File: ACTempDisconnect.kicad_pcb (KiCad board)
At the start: 4 copper layers, 120 x 99.5 mm, 49 parts, among them J1001 Conn_01x03_Female, J1002 NTC_Connection, J1003 Conn_01x02_Female, J1004 Conn_01x03_Female, J1005 Conn_01x02_Female, J2001 TAG_CONNECT, K1001 ADW1103HLW, K1002 ADW1103HLW, K1003 ADW1103HLW, K1004 ADW1103HLW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

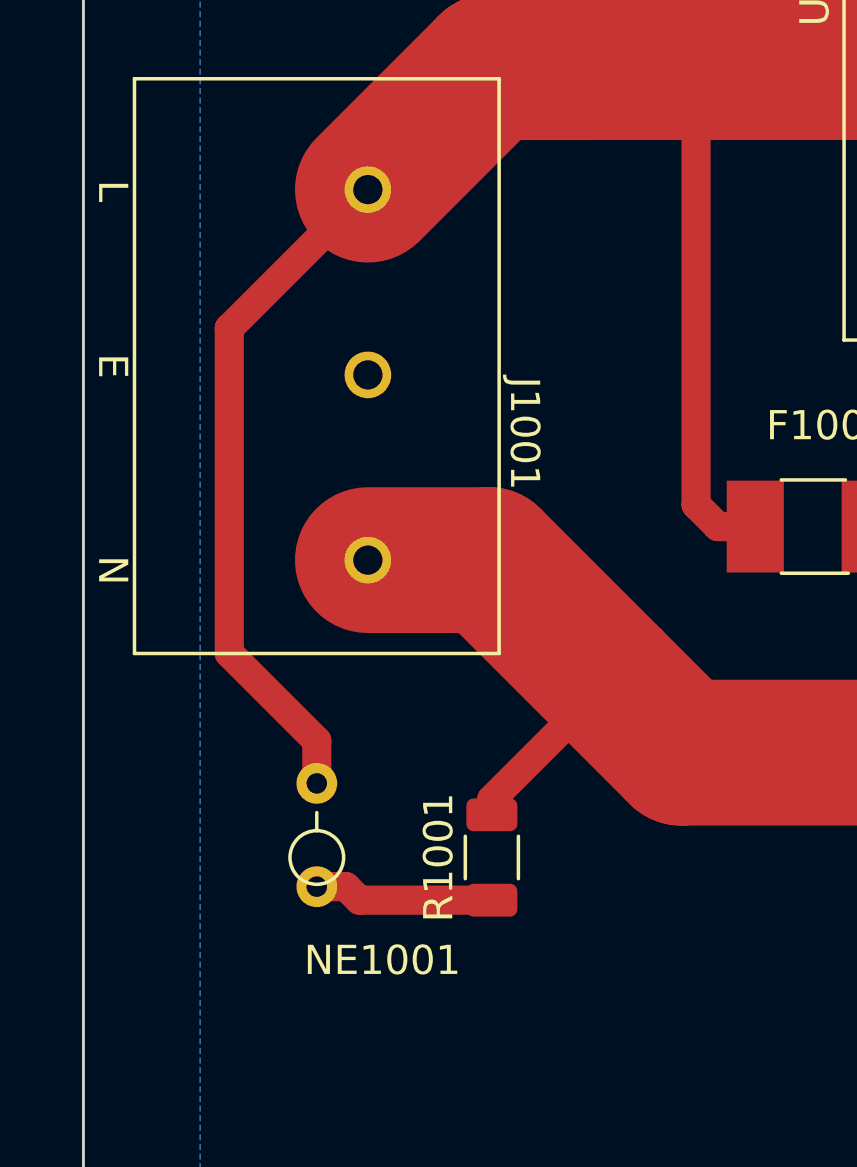
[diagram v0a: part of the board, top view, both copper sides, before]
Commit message: Removed Neon from V2
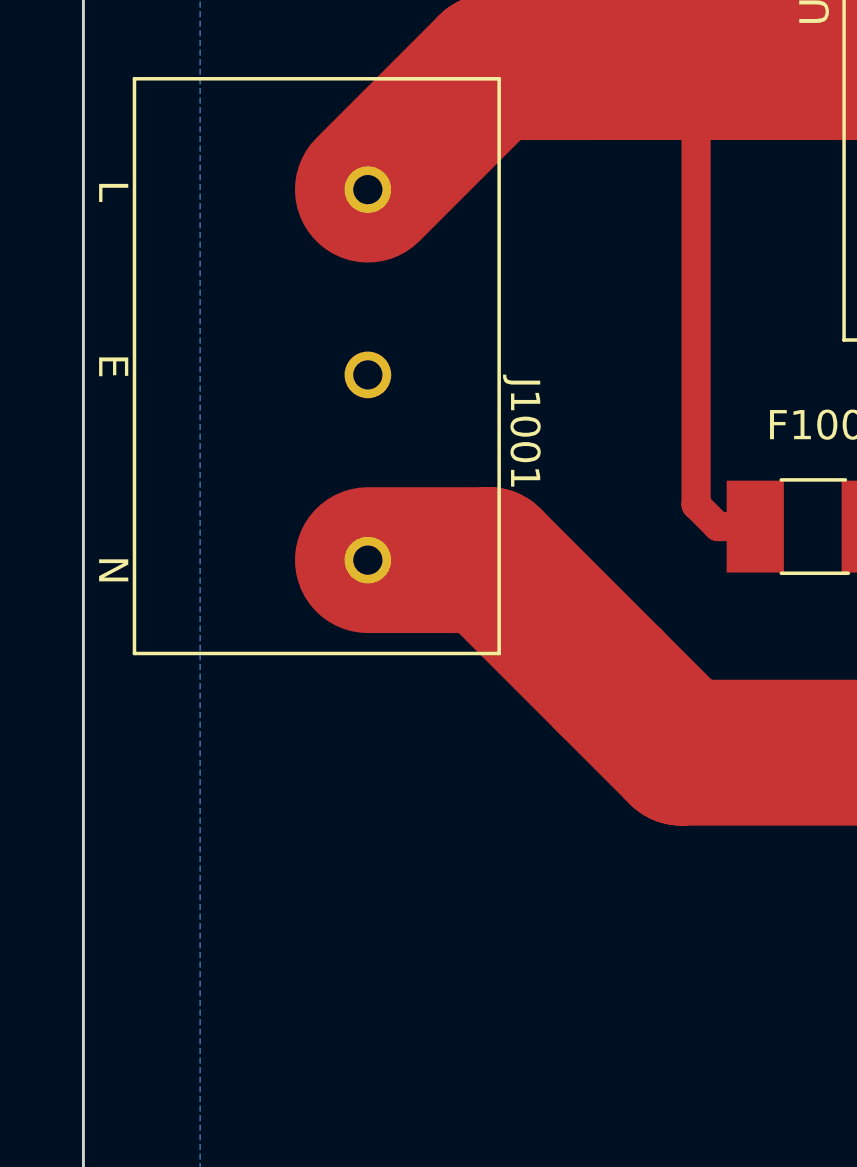
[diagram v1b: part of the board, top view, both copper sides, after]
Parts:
- removed NE1001: Lamp_Neon, Resistor_THT:R_Axial_DIN0204_L3.6mm_D1.6mm_P2.54mm_Vertical
- removed R1001: 33k, Resistor_SMD:R_1206_3216Metric
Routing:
- net /L_IN: track 145.5 -> 121.9 mm
- net /N_IN: track 164.1 -> 157.8 mm
- net /_NEON: track 6.19 -> 0.00 mm

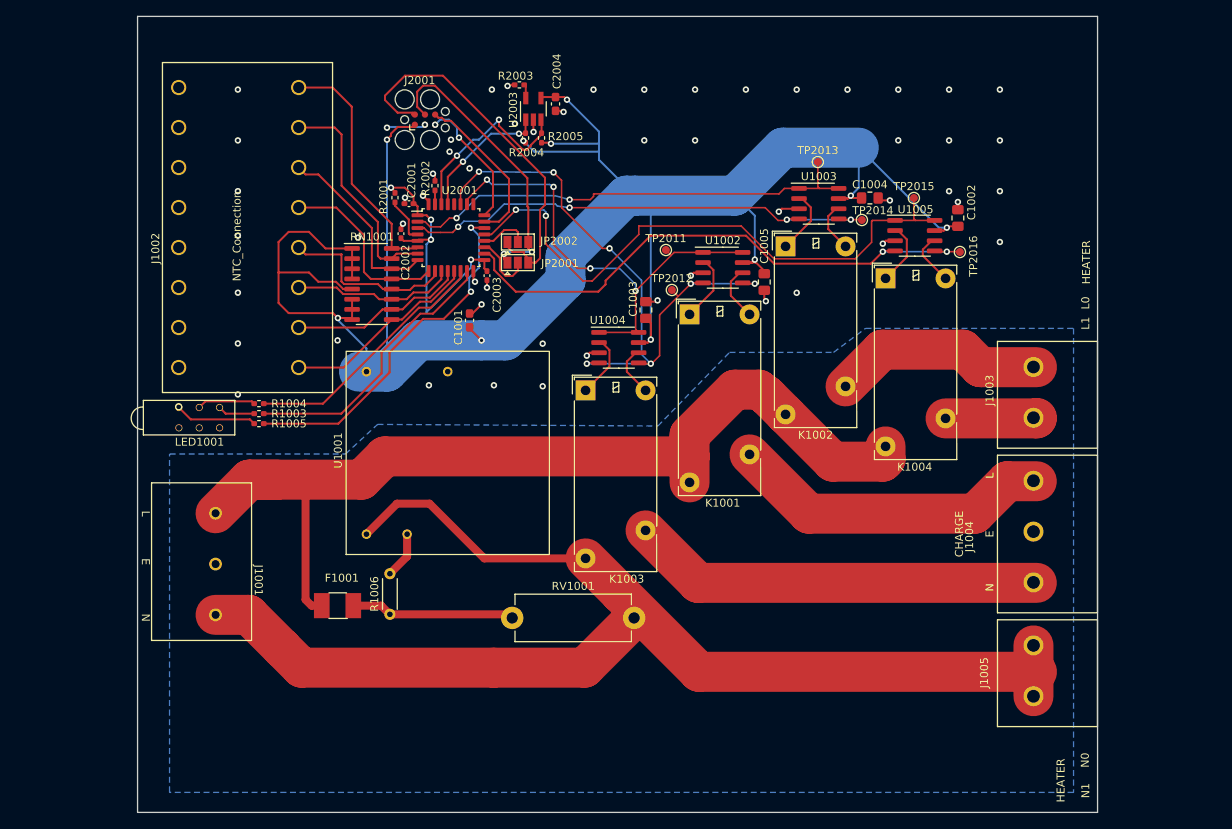
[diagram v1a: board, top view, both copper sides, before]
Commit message: WIP - Redo of A/C Layout
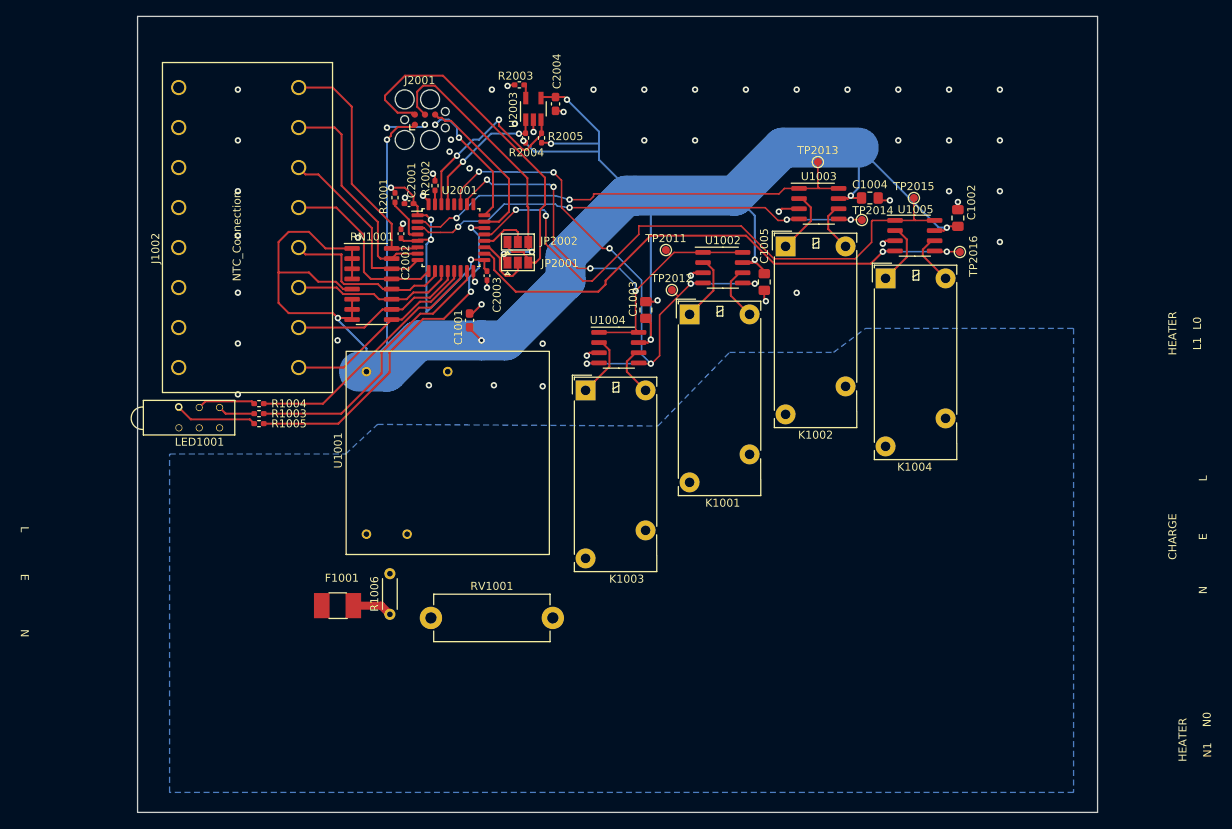
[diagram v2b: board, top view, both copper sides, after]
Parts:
- removed J1001, J1004: Conn_01x03_Female, Library:OSTT7030150
- removed J1003, J1005: Conn_01x02_Female, Library:OSTT7020150
- moved RV1001 10.2 mm to (86.7, 157.2)
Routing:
- net /N_IN: track 157.8 -> 0.00 mm
- net /L_IN: track 121.9 -> 0.00 mm
- net /N_OUT: track 51.6 -> 0.00 mm
- net /L_OUT: track 40.7 -> 0.00 mm
- net /L_HEATER0: track 26.7 -> 0.00 mm
- net /_AC_FUSE: track 20.5 -> 5.02 mm
- net /L_HEATER1: track 11.4 -> 0.00 mm
- net /ACIN_L: track 5.83 -> 0.00 mm

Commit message: Rev 2
Simplified the layout. Reduced down to 2 layers.
Added top/bottom traces to split the current.
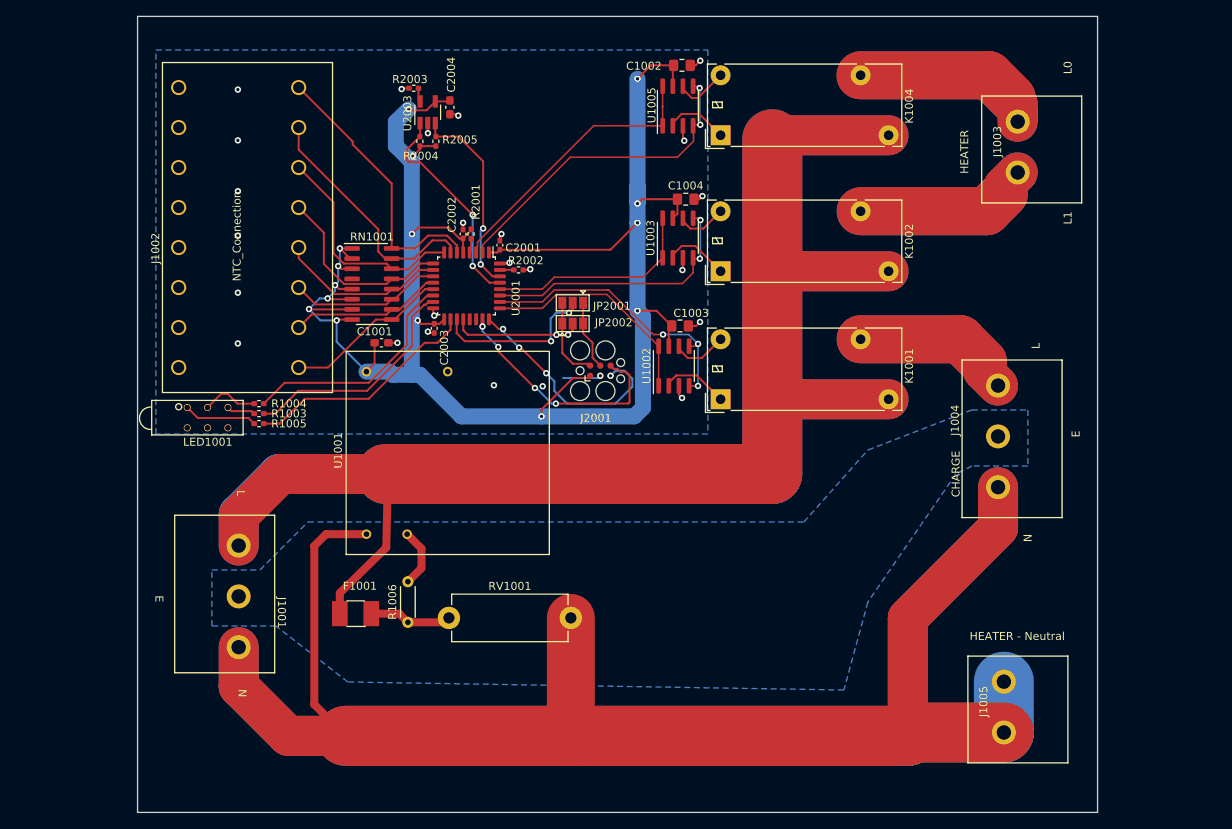
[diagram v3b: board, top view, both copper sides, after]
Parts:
- removed C1005: 2.2u, Capacitor_SMD:C_0805_2012Metric_Pad1.18x1.45mm_HandSolder
- removed K1003: ADW1103HLW, Relay_THT:Relay_1P1T_NO_10x24x18.8mm_Panasonic_ADW11xxxxW_THT
- removed TP2011, TP2012, TP2013, TP2014, TP2015, TP2016: TestPoint, TestPoint:TestPoint_Pad_D1.0mm
- removed U1004: DMHC4035LSD, Package_SO:SOIC-8_3.9x4.9mm_P1.27mm
- added J1001: Conn_01x03_Female, Library:OSTT7030150, F.Cu at (62.6, 148.2)
- added J1003: Conn_01x02_Female, Library:OSTT7020150, F.Cu at (159.3, 101.2)
- added J1004: Conn_01x03_Female, Library:OSTT7030150, F.Cu at (157.6, 140.8)
- added J1005: Conn_01x02_Female, Library:OSTT7020150, F.Cu at (157.6, 171.2)
- moved C1002 39.4 mm to (118.0, 88.1), turned to 0 degrees
- moved J2001 38.3 mm to (107.9, 126.3)
- moved U1005 33.8 mm to (117.5, 93.2), turned to 90 degrees
- moved K1004 27.3 mm to (122.9, 96.9), turned to 90 degrees
- moved C1004 23.0 mm to (118.5, 104.8)
- moved U1003 18.1 mm to (117.5, 109.7), turned to 90 degrees
- moved R2002 14.8 mm to (97.6, 113.7), turned to 0 degrees
- moved U1002 13.7 mm to (117.0, 125.7), turned to 90 degrees
- moved R2003 13.2 mm to (84.5, 91.0)
- moved U2003 13.2 mm to (86.3, 94.0)
- moved C2004 13.2 mm to (89.0, 93.4)
- moved R2004 13.2 mm to (85.3, 97.6)
- moved R2005 13.2 mm to (87.3, 97.6)
- moved C2001 12.5 mm to (95.3, 110.6), turned to 90 degrees
- moved JP2002 12.3 mm to (104.4, 120.4)
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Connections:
- U2001 pad 18: /HR1- -> /G
- U2001 pad 2: /HR0+ -> /HR1-
- U2001 pad 21: /HR1+ -> unconnected-(U2001-Pad21)
- U2001 pad 22: /G -> unconnected-(U2001-Pad22)
- U2001 pad 25: unconnected-(U2001-Pad25) -> /CR+
- U2001 pad 26: /CR+ -> /CR-
- U2001 pad 27: /CR- -> /HR0-
- U2001 pad 28: unconnected-(U2001-Pad28) -> /HR0+
- U2001 pad 3: /HR0- -> /HR1+
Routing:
- net /L_IN: track 0.00 -> 374.7 mm
- net /N_IN: track 0.00 -> 331.7 mm
- net +3V3: track 312.1 -> 235.8 mm, vias 14 -> 15
- net /L_HEATER1: track 0.00 -> 46.7 mm
- net /L_HEATER0: track 0.00 -> 44.4 mm
- net /CR-: track 79.3 -> 35.8 mm, vias 7 -> 3
- net /L_OUT: track 0.00 -> 40.4 mm
- net /HR1+: track 75.2 -> 35.6 mm, vias 2 -> 0
- net /MCU/UART_TX: track 48.2 -> 10.8 mm
- net /HR0+: track 58.7 -> 27.2 mm, vias 2 -> 0
- net /CR+: track 59.7 -> 28.9 mm, vias 4 -> 0
- net /HR1-: track 70.6 -> 41.1 mm
- net /MCU/UART_RX: track 36.5 -> 8.75 mm, vias 2 -> 0
- net /HR0-: track 61.2 -> 34.1 mm, vias 4 -> 2
- net GND: track 41.9 -> 24.5 mm, vias 56 -> 25
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- added copper zone on B.Cu, net GND
- removed copper zone on In1.Cu, net GND
- removed copper zone on In2.Cu, net GND
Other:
- copper layers 4 -> 2
- board text added: "HEATER - Neutral"
- board text removed: "N0"
- board text removed: "N1"

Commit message: 8 to 4 NTC
Reduced down from 8 to 4 NTCs, for cost down and packaging
considerations.
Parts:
- J1002: value NTC_Connection -> Conn_02x04_Counter_Clockwise; footprint Library:736-108 -> Library:736-104
- RN1001: value R_Pack08 -> R_Pack04; footprint Package_SO:SOIC-16_3.9x9.9mm_P1.27mm -> Resistor_SMD:R_Array_Convex_4x1206
- moved J1002 31.9 mm to (73.3, 99.7), turned to -90 degrees
- moved LED1001 6.20 mm to (61.6, 127.2)
- moved R1003 6.20 mm to (65.5, 125.5)
- moved R1004 6.20 mm to (65.5, 124.2)
- moved R1005 6.20 mm to (65.5, 126.7)
- moved RN1001 2.75 mm to (79.3, 112.7)
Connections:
- J1002 pad 1: GND -> /MCU/NTC0
- J1002 pad 2: GND -> /MCU/NTC1
- J1002 pad 3: GND -> /MCU/NTC2
- J1002 pad 4: GND -> /MCU/NTC3
- RN1001 pad 5: +3V3 -> /MCU/NTC3
- RN1001 pad 6: +3V3 -> /MCU/NTC2
- RN1001 pad 7: +3V3 -> /MCU/NTC1
- RN1001 pad 8: +3V3 -> /MCU/NTC0
- U2001 pad 10: /MCU/NTC4 -> unconnected-(U2001-Pad10)
- U2001 pad 11: /MCU/NTC5 -> unconnected-(U2001-Pad11)
- U2001 pad 12: /MCU/NTC6 -> unconnected-(U2001-Pad12)
- U2001 pad 13: /MCU/NTC7 -> unconnected-(U2001-Pad13)
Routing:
- net +3V3: track 235.8 -> 214.2 mm, vias 15 -> 10
- net /MCU/NTC4: track 21.3 -> 0.00 mm
- net /MCU/NTC7: track 20.9 -> 0.00 mm
- net GND: track 24.5 -> 44.5 mm, vias 25 -> 32
- net /MCU/NTC5: track 19.1 -> 0.00 mm
- net /MCU/NTC6: track 19.1 -> 0.00 mm
- net /MCU/NTC2: track 28.0 -> 18.7 mm
- net /MCU/NTC0: track 35.2 -> 26.3 mm
- net /MCU/NTC1: track 31.1 -> 23.6 mm
- net /MCU/NTC3: track 24.1 -> 17.9 mm
- net /R: track 29.1 -> 24.0 mm
- net /Y: track 28.9 -> 23.9 mm
- net /G: track 29.5 -> 27.1 mm

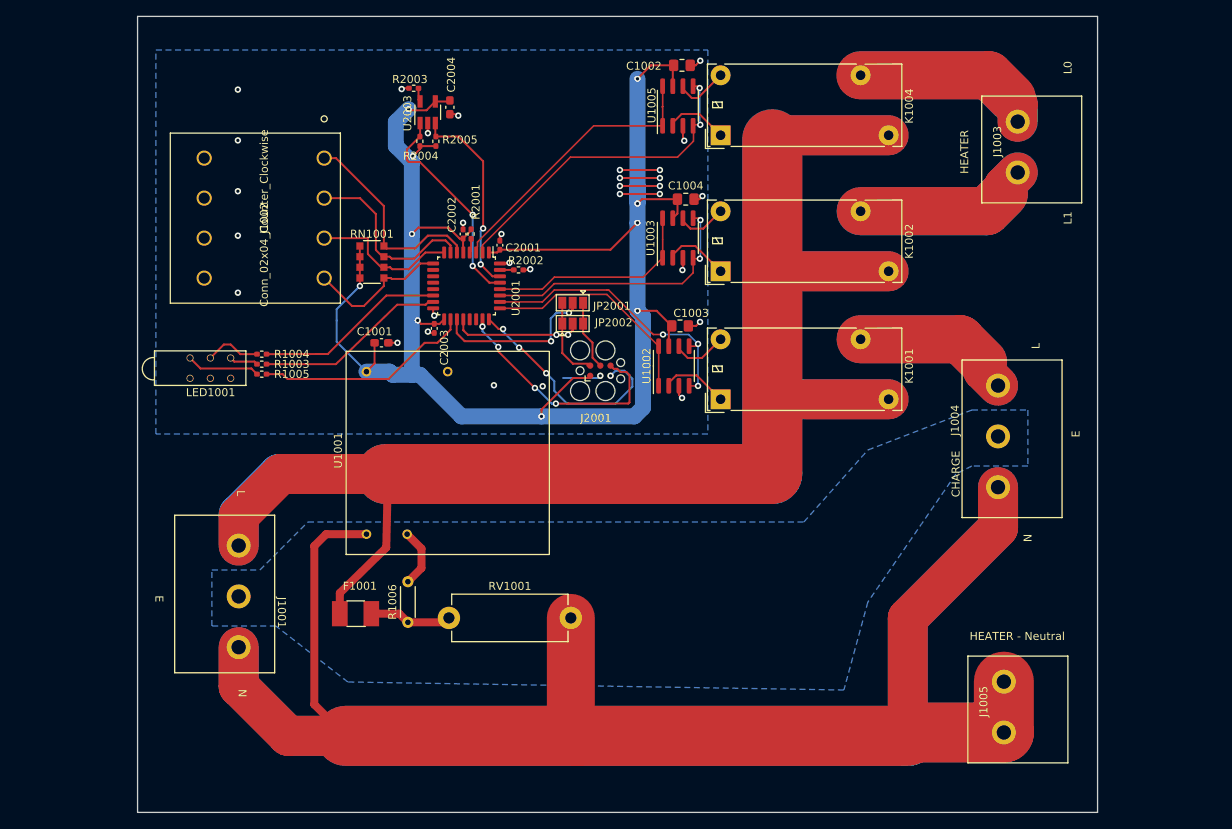
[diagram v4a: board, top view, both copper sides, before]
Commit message: New Layout for Battery Charge Controller
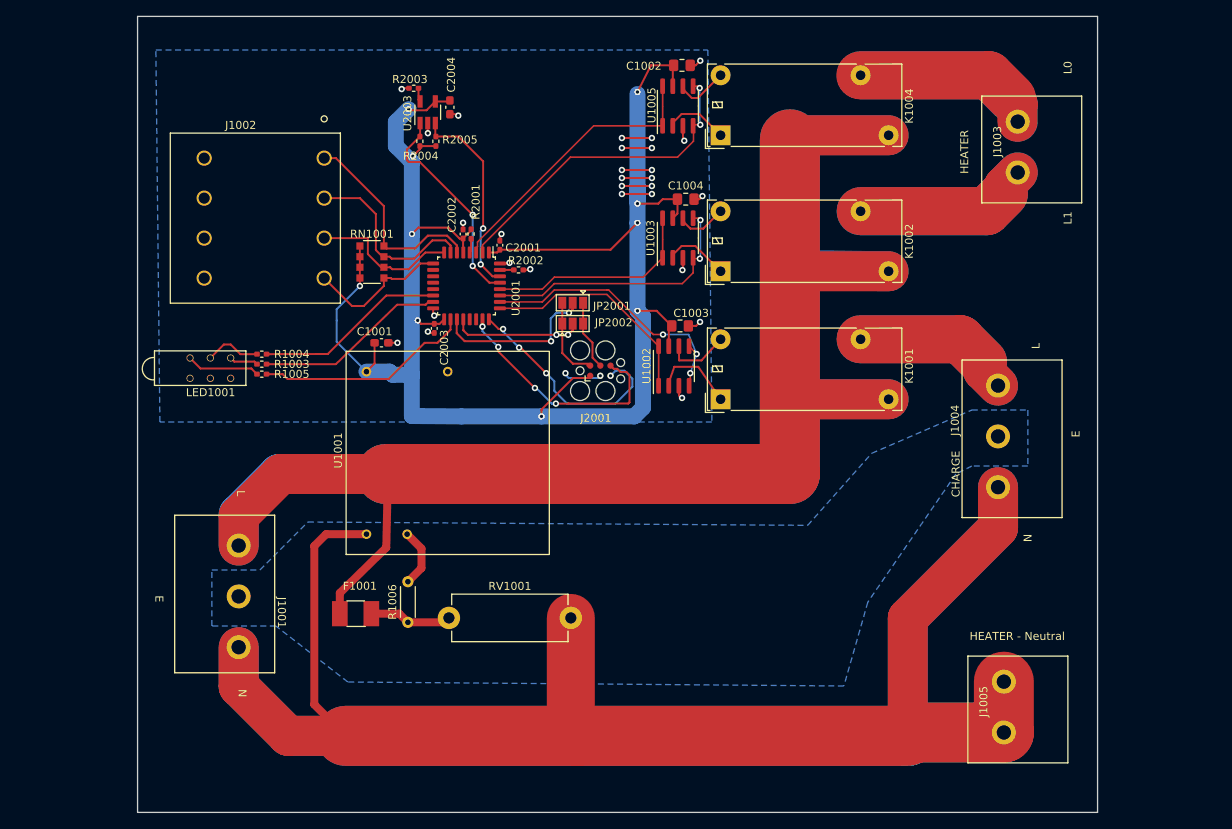
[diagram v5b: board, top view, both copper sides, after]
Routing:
- net GND: track 44.5 -> 47.1 mm, vias 32 -> 30
- net +3V3: track 214.2 -> 216.5 mm
- net Net-(K1001-Pad1): track 8.10 -> 10.0 mm
- net /_AC_FUSE: track 11.0 -> 9.60 mm
- net /CR-: track 35.8 -> 34.5 mm
- net Net-(K1001-Pad6): track 6.63 -> 7.76 mm
- net /L_IN: track 374.7 -> 373.6 mm
- net /CR+: track 28.9 -> 28.2 mm
